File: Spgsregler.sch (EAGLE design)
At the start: 13 parts, among them X1 22-23-2101, X2 22-23-2101, X4 22-23-2031, X5 22-23-2031

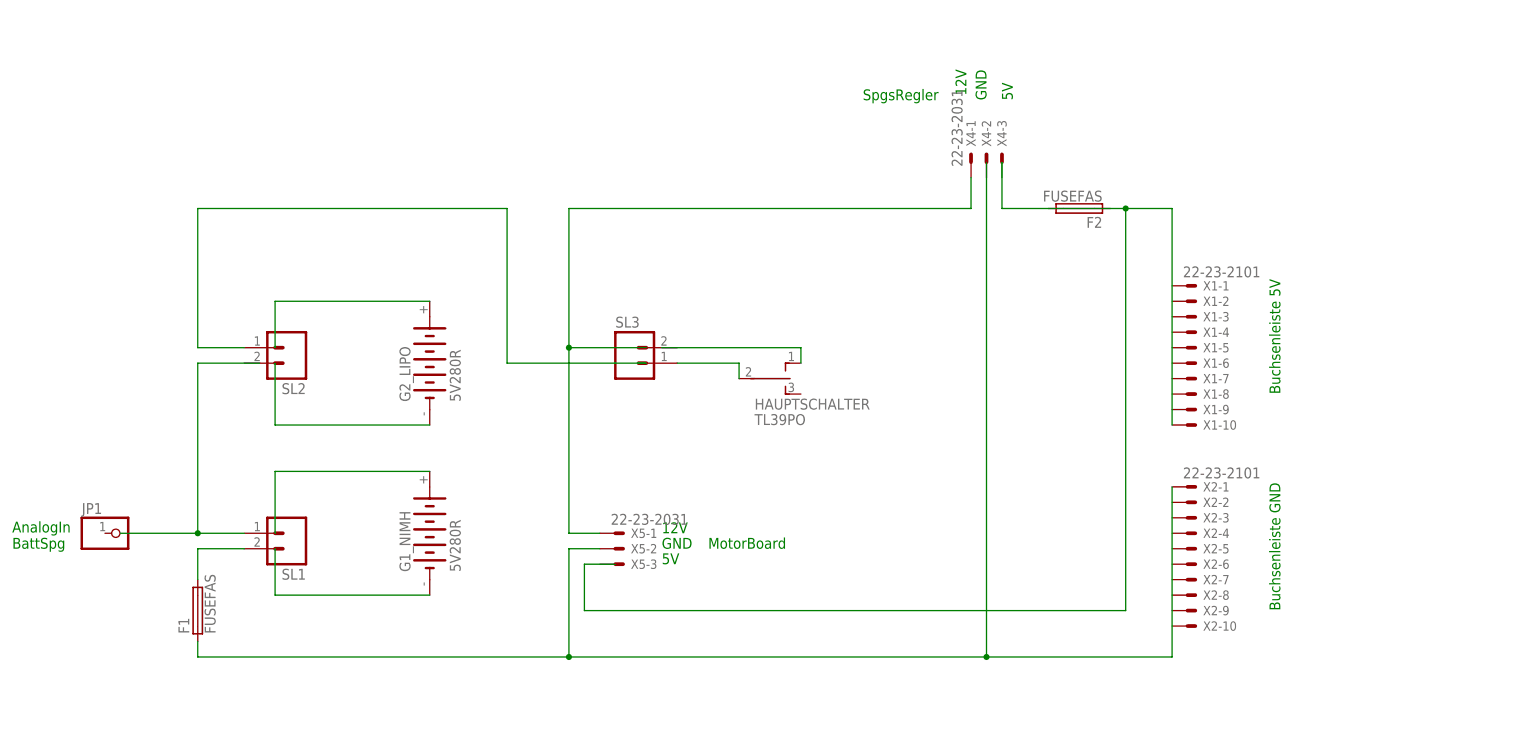
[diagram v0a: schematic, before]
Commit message: 
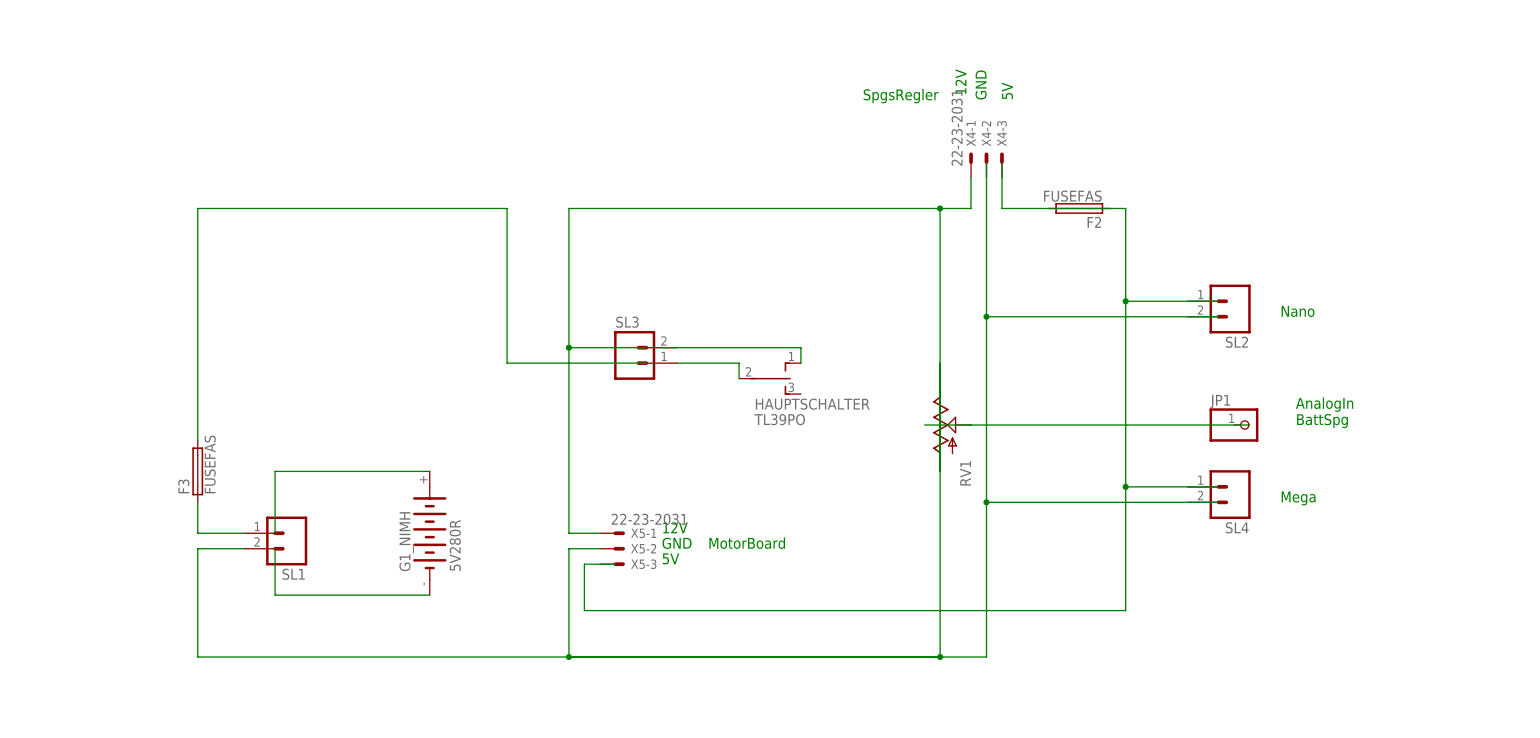
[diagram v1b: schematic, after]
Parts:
- removed F1: FUSEFAS, fuse:FUSEFAS
- removed G2_LIPO: 5V280R, battery:5V280R
- removed X1, X2: 22-23-2101, con-molex:22-23-2101
- added F3: FUSEFAS, fuse:FUSEFAS
- added RV1: (no value), SparkFun-Electromechanical:POTTRIM
- added SL4: (no value), con-amp-quick:M02
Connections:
- removed net N$3: G2_LIPO.+
- removed net N$7: F1.2, SL1.2
- net N$11: now also SL1.2, X5-2.S; no longer X4-1.S, X5-1.S
- net N$12: no longer X1-10.S
- net N$4: now also F3.1, SL1.1; no longer G2_LIPO.-
- net N$5: now also RV1.A, X4-1.S, X5-1.S; no longer SL1.1
- net N$6: now also RV1.S; no longer F1.1, X2-1.S, X5-2.S
- net N$8: now also F3.2; no longer SL2.1
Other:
- note added: "Mega"
- note added: "Nano"
- note removed: "Buchsenleiste 5V"
- note removed: "Buchsenleiste GND"
- moved on the sheet: JP1, SL2

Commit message: 
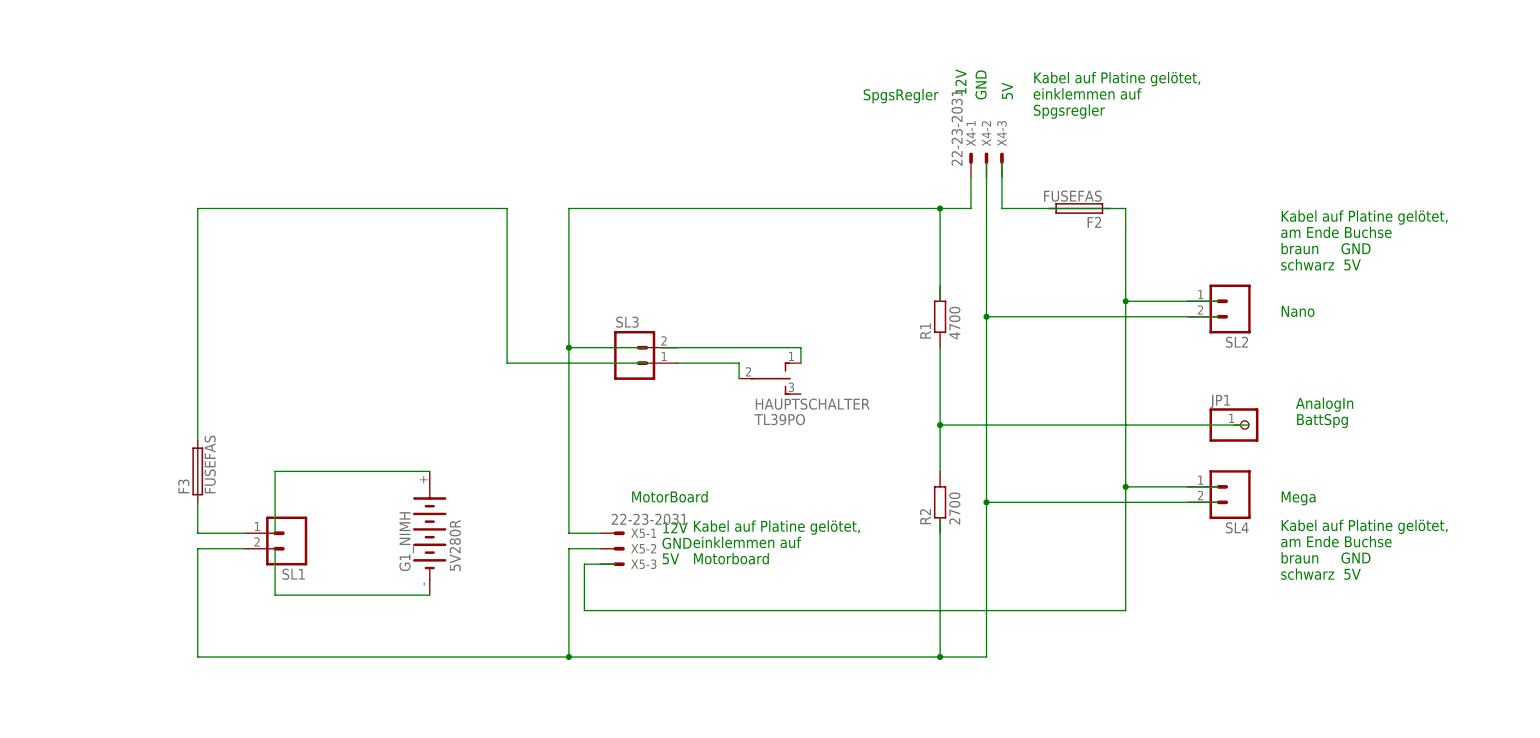
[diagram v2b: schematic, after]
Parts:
- removed RV1: (no value), SparkFun-Electromechanical:POTTRIM
- added R1: 4700, rcl:R-EU_0207/10
- added R2: 2700, rcl:R-EU_0207/10
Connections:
- removed net N$6: RV1.S
- new net N$3: R1.1, R2.2
- net N$5: no longer RV1.A
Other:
- note added: "Kabel auf Platine gelötet, am Ende Buchse braun GND schwarz 5V"
- note added: "Kabel auf Platine gelötet, einklemmen auf Motorboard"
- note added: "Kabel auf Platine gelötet, einklemmen auf Spgsregler"
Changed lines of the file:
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@@
 <layer number="113" name="IDFDebug" color="4" fill="1" visible="no" active="yes"/>
 <layer number="116" name="Patch_BOT" color="9" fill="4" visible="no" active="yes"/>
+<layer number="118" name="Rect_Pads" color="7" fill="1" visible="no" active="no"/>
 <layer number="121" name="_tsilk" color="7" fill="1" visible="no" active="yes"/>
 <layer number="122" name="_bsilk" color="7" fill="1" visible="no" active="yes"/>
@@
 <layer number="230" name="230bmp" color="7" fill="1" visible="yes" active="yes"/>
 <layer number="231" name="231bmp" color="7" fill="1" visible="yes" active="yes"/>
+<layer number="232" name="Eagle3D_PG2" color="7" fill="1" visible="no" active="no"/>
+<layer number="233" name="Eagle3D_PG3" color="7" fill="1" visible="no" active="no"/>
 <layer number="248" name="Housing" color="7" fill="1" visible="no" active="yes"/>
 <layer number="249" name="Edge" color="7" fill="1" visible="no" active="yes"/>
@@
 <part name="SL4" library="con-amp-quick" deviceset="M02" device=""/>
 <part name="F3" library="fuse" deviceset="FUSE" device="FAS"/>
-<part name="RV1" library="SparkFun-Electromechanical" deviceset="POT" device="TRIM"/>
+<part name="R1" library="rcl" deviceset="R-EU_" device="0207/10" value="4700"/>
+<part name="R2" library="rcl" deviceset="R-EU_" device="0207/10" value="2700"/>
 </parts>
 <sheets>
 <sheet>
 <plain>
-<text x="88.9" y="22.86" size="1.778" layer="91">MotorBoard</text>
+<text x="76.2" y="30.48" size="1.778" layer="91">MotorBoard</text>
 <text x="185.42" y="43.18" size="1.778" layer="91">AnalogIn
 BattSpg</text>
@@
 <text x="182.88" y="30.48" size="1.778" layer="91">Mega</text>
 <text x="182.88" y="60.96" size="1.778" layer="91">Nano</text>
+<text x="182.88" y="68.58" size="1.778" layer="91">Kabel auf Platine gelötet,
+am Ende Buchse
+braun     GND
+schwarz  5V</text>
+<text x="182.88" y="17.78" size="1.778" layer="91">Kabel auf Platine gelötet,
+am Ende Buchse
+braun     GND
+schwarz  5V</text>
+<text x="86.36" y="20.32" size="1.778" layer="91">Kabel auf Platine gelötet,
+einklemmen auf
+Motorboard</text>
+<text x="142.24" y="93.98" size="1.778" layer="91">Kabel auf Platine gelötet,
+einklemmen auf
+Spgsregler</text>
 </plain>
 <instances>
@@
 <instance part="SL4" gate="G$1" x="175.26" y="33.02" rot="R180"/>
 <instance part="F3" gate="G$1" x="5.08" y="35.56" rot="R90"/>
-<instance part="RV1" gate="G$1" x="127" y="43.18"/>
+<instance part="R1" gate="G$1" x="127" y="60.96" rot="R90"/>
+<instance part="R2" gate="G$1" x="127" y="30.48" rot="R90"/>
 </instances>
 <busses>
@@
 </segment>
 </net>
-<net name="N$6" class="0">
-<segment>
-<pinref part="RV1" gate="G$1" pin="S"/>
-<wire x1="132.08" y1="43.18" x2="124.46" y2="43.18" width="0.1524" layer="91"/>
-<wire x1="177.8" y1="43.18" x2="132.08" y2="43.18" width="0.1524" layer="91"/>
-</segment>
-</net>
 <net name="N$5" class="0">
 <segment>
-<pinref part="RV1" gate="G$1" pin="A"/>
-<wire x1="127" y1="35.56" x2="127" y2="53.34" width="0.1524" layer="91"/>
 <wire x1="78.74" y1="55.88" x2="66.04" y2="55.88" width="0.1524" layer="91"/>
 <wire x1="66.04" y1="55.88" x2="66.04" y2="78.74" width="0.1524" layer="91"/>
@@
 <pinref part="X4" gate="-1" pin="S"/>
 <wire x1="132.08" y1="78.74" x2="132.08" y2="83.82" width="0.1524" layer="91"/>
-<wire x1="127" y1="35.56" x2="127" y2="78.74" width="0.1524" layer="91"/>
+<wire x1="127" y1="63.5" x2="127" y2="78.74" width="0.1524" layer="91"/>
 <junction x="127" y="78.74"/>
 </segment>
@@
 <wire x1="134.62" y1="5.08" x2="127" y2="5.08" width="0.1524" layer="91"/>
 <pinref part="X5" gate="-2" pin="S"/>
-<wire x1="127" y1="5.08" x2="66.04" y2="5.08" width="0.1524" layer="91"/>
 <wire x1="134.62" y1="30.48" x2="134.62" y2="5.08" width="0.1524" layer="91"/>
 <wire x1="172.72" y1="30.48" x2="134.62" y2="30.48" width="0.1524" layer="91"/>
 <wire x1="5.08" y1="22.86" x2="5.08" y2="5.08" width="0.1524" layer="91"/>
-<wire x1="127" y1="38.1" x2="127" y2="5.08" width="0.1524" layer="91"/>
 <wire x1="127" y1="5.08" x2="66.04" y2="5.08" width="0.1524" layer="91"/>
 <wire x1="134.62" y1="60.96" x2="134.62" y2="30.48" width="0.1524" layer="91"/>
@@
 <junction x="134.62" y="30.48"/>
 <junction x="134.62" y="60.96"/>
-</segment>
-</net>
+<wire x1="127" y1="5.08" x2="127" y2="27.94" width="0.1524" layer="91"/>
+</segment>
+</net>
+<net name="N$3" class="0">
+<segment>
+<pinref part="R2" gate="G$1" pin="2"/>
+<pinref part="R1" gate="G$1" pin="1"/>
+<wire x1="127" y1="35.56" x2="127" y2="43.18" width="0.1524" layer="91"/>
+<wire x1="127" y1="43.18" x2="127" y2="55.88" width="0.1524" layer="91"/>
+<wire x1="177.8" y1="43.18" x2="127" y2="43.18" width="0.1524" layer="91"/>
+<junction x="127" y="43.18"/>
+</segment>
+</net>
